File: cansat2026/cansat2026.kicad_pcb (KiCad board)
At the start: 2 copper layers, 119 parts, among them J102 MCU_UART_Conn, J103 MCU_CAM_UART_Conn, J104 920MHz_Conn, J105 I2C_Conn, J106 I2C_Conn, J117 CAM_Conn, J121 MCU_Power, J122 MCU_Power, J124 Motor_Power, J126 Micro_SD_Card_Det_Hirose_DM3AT, J201 FlightPin, J202 Heater, J301 Battery, J302 Battery, J401 M_Power_Conn, J402 M1, J403 M2, J801 Conn_Coaxial, Q301 2SB1198K, Q302 2SB1198K, Q303 2N7002, Q304 2SB1198K, Q305 2N7002, Q306 2SC2412K, Q307 PJA3404A, Q308 PJA3404A, U101 ESP32-S3-WROOM-1U-N4R8, U102 ESP32-S3-WROOM-1U-N4R8, U201 TPS564252, U202 TPS564252, U203 TPS22810DBV, U301 S-8209ABB-T8T1U, U302 S-8209ABB-T8T1U, U401 DRV8835, U601 AE-BME280, U701 BNO055 FusionModule, U801 NEO-M9N

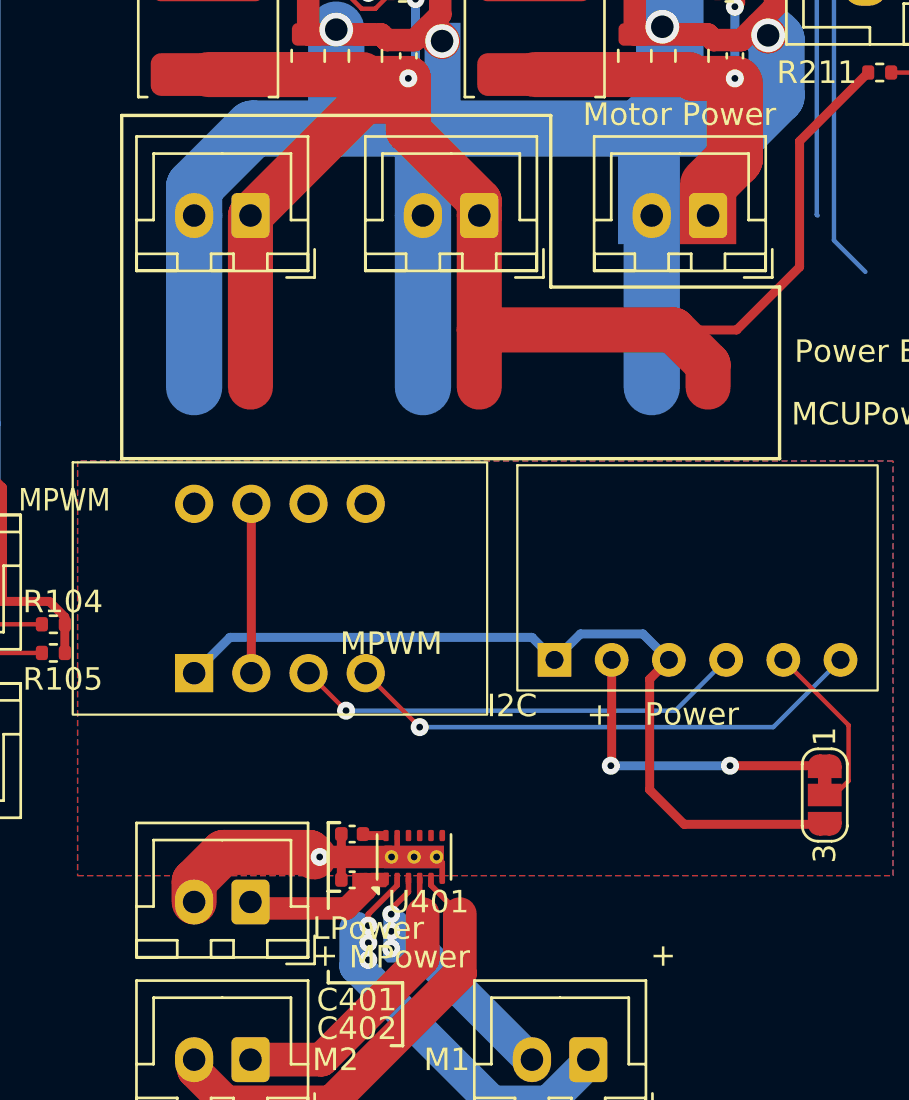
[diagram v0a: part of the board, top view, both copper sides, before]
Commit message: Update: MCUシートを作成
MCU部分を分けた
あとでFPGAつけるかもしれないしね
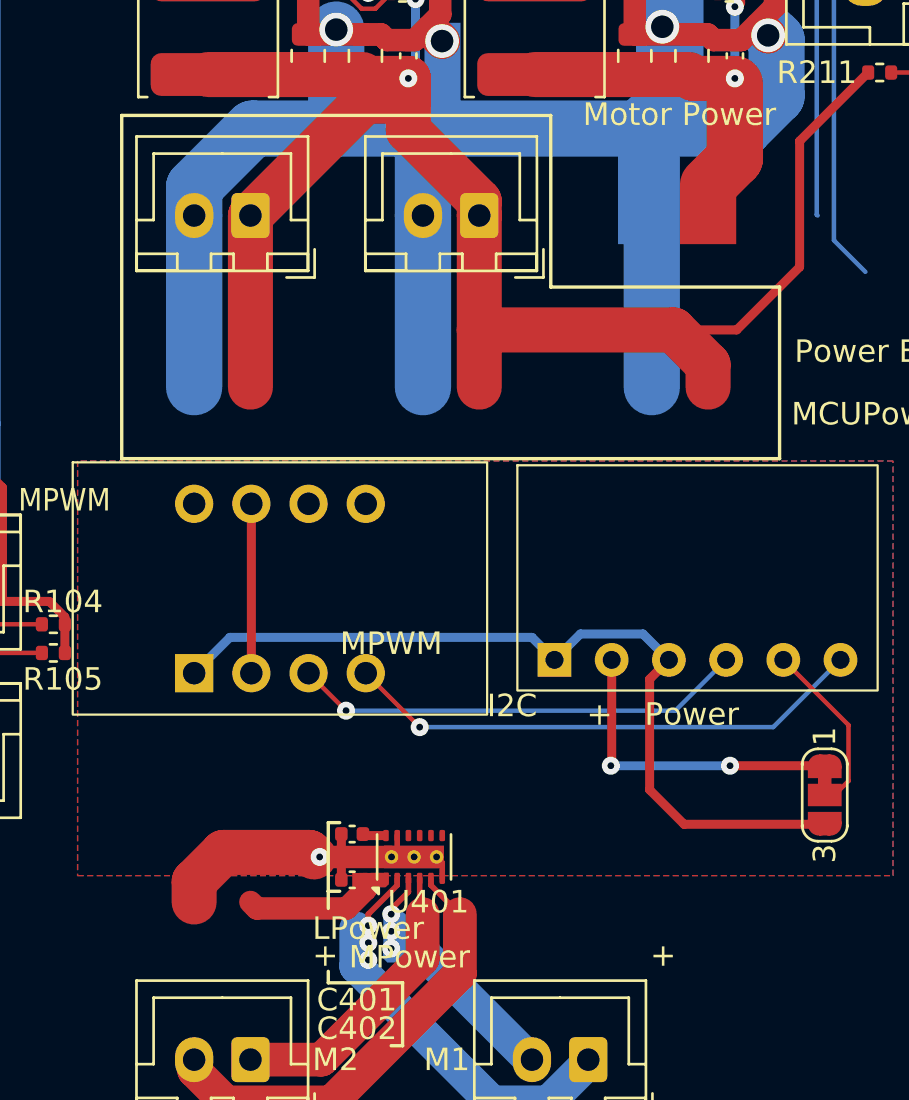
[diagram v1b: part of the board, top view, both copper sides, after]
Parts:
- removed J124: Motor_Power, Connector_JST:JST_XH_B2B-XH-A_1x02_P2.50mm_Vertical
- removed J401: M_Power_Conn, Connector_JST:JST_XH_B2B-XH-A_1x02_P2.50mm_Vertical
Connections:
- net /I2C2SCL renamed /MCU/I2C2SCL
- net /I2C2SDA renamed /MCU/I2C2SDA
- C209 pad 1: /Power/3V -> /MPWR
- C210 pad 1: /Power/3V -> /MPWR
- C211 pad 1: /Power/3V -> /MPWR
- C212 pad 1: /Power/3V -> /MPWR
- C402 pad 1: Net-(J401-Pin_1) -> /MPWR
- L202 pad 2: /Power/3V -> /MPWR
- R207 pad 1: /Power/3V -> /MPWR
- R208 pad 1: /Power/3V -> /MPWR
- U401 pad 1: Net-(J401-Pin_1) -> /MPWR
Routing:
- net /MPWR: track 0.00 -> 29.8 mm, vias 0 -> 3
- net /Power/3V: track 23.9 -> 0.00 mm, vias 3 -> 0
- net Net-(J401-Pin_1): track 5.82 -> 0.00 mm

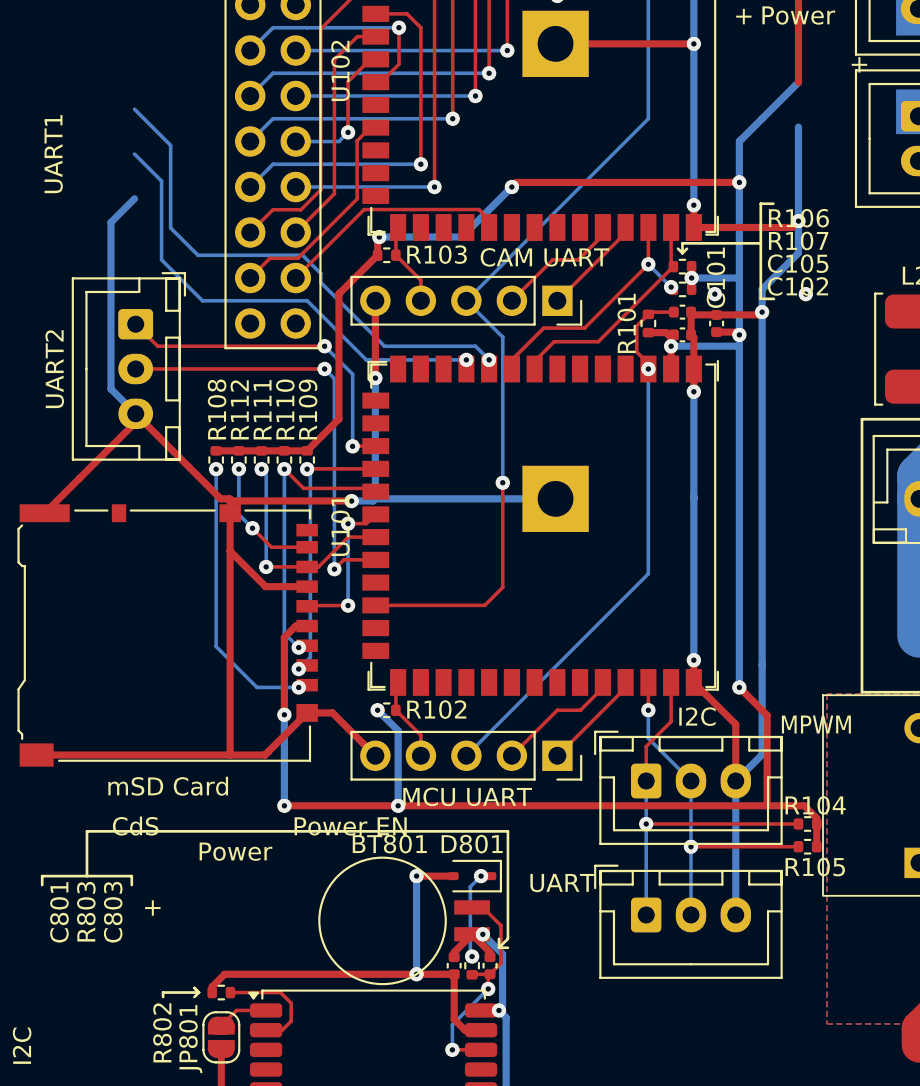
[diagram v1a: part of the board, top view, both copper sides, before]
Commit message: Update: ラベルをワイヤーにした
ラベルが衝突してERCが出たから
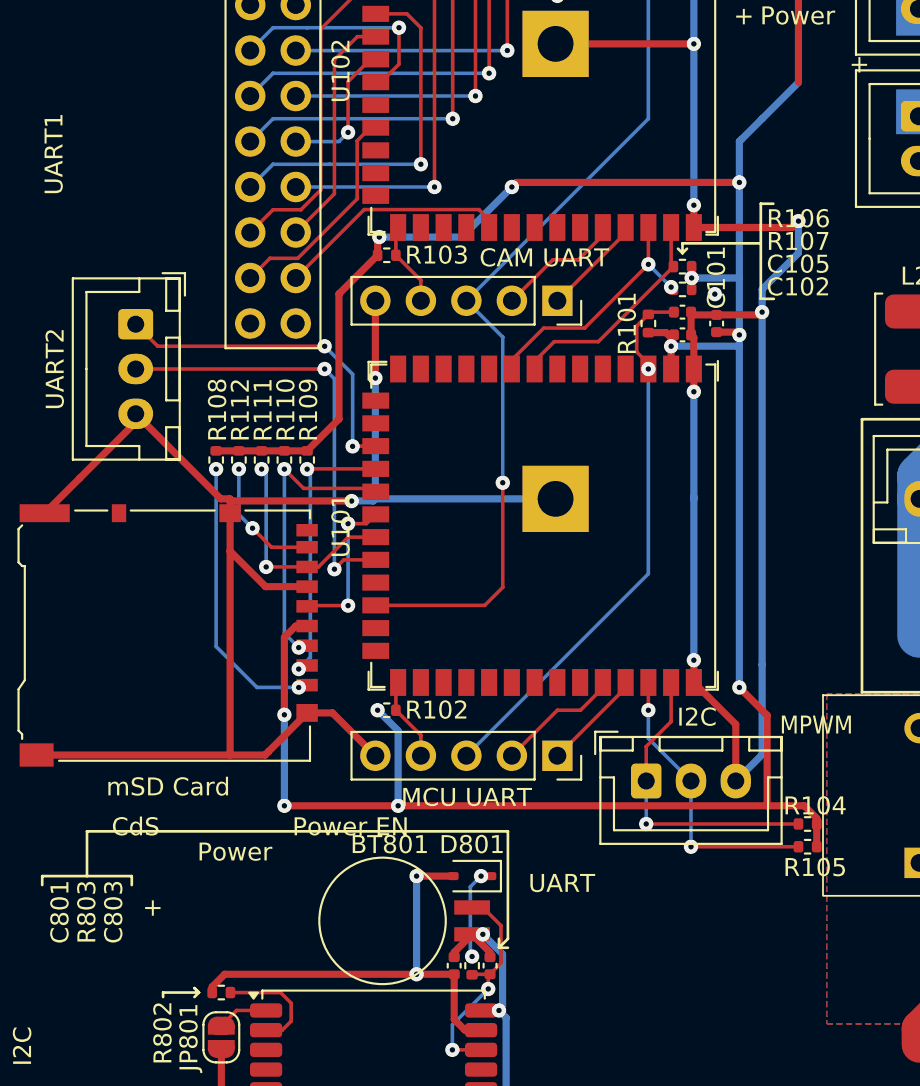
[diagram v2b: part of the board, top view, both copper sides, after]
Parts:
- removed J106: I2C_Conn, Connector_JST:JST_XH_B3B-XH-A_1x03_P2.50mm_Vertical
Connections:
- net /FP renamed /MCU/FP
- net /MA1 renamed /MCU/MA1
- net /MA2 renamed /MCU/MA2
- net /MB1 renamed /MCU/MB1
- net /MB2 renamed /MCU/MB2
- net /MPWR renamed /MD/MPWR
- net /Motor_P_EN renamed /MCU/Motor_P_EN
- net /PC_Sep renamed /MCU/PC_Sep
- net /U1RXD renamed /GPS/GPS_TX
- net /U1TXD renamed /GPS/GPS_RX
- R104 pad 2: /I2C1SDA -> /MCU/I2C1SDA
- R105 pad 2: /I2C1SCL -> /MCU/I2C1SCL
- U101 pad 38: /I2C1SCL -> /MCU/I2C1SCL
- U101 pad 39: /I2C1SDA -> /MCU/I2C1SDA
- U601 pad 4: /I2C1SDA -> /MCU/I2C1SDA
- U601 pad 6: /I2C1SCL -> /MCU/I2C1SCL
- U701 pad 3: /I2C1SDA -> /MCU/I2C1SDA
- U701 pad 4: /I2C1SCL -> /MCU/I2C1SCL
- U801 pad 18: /I2C1SDA -> /MCU/I2C1SDA
- U801 pad 19: /I2C1SCL -> /MCU/I2C1SCL
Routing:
- net /GPS/GPS_RX: track 29.1 -> 0.00 mm, vias 1 -> 0
- net /I2C1SCL: track 43.3 -> 16.2 mm, vias 3 -> 2
- net /GPS/GPS_TX: track 26.4 -> 0.00 mm, vias 1 -> 0
- net GND: track 515.5 -> 489.7 mm, vias 54 -> 53
- net /I2C1SDA: track 42.2 -> 17.0 mm, vias 2 -> 1
- net /MCU/I2C1SCL: track 0.00 -> 23.3 mm, vias 0 -> 1
- net /MCU/I2C1SDA: track 0.00 -> 20.2 mm, vias 0 -> 1

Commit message: Update: 完成した
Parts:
- removed C103: 10uF, Capacitor_SMD:C_0402_1005Metric
- removed C104: 100nF, Capacitor_SMD:C_0402_1005Metric
- removed C105: 1uF, Capacitor_SMD:C_0402_1005Metric
- removed J117: CAM_Conn, Connector_PinHeader_2.54mm:PinHeader_2x10_P2.54mm_Vertical
- removed J121, J122: MCU_Power, Connector_JST:JST_XH_B2B-XH-A_1x02_P2.50mm_Vertical
- removed J126: Micro_SD_Card_Det_Hirose_DM3AT, Connector_Card:microSD_HC_Hirose_DM3AT-SF-PEJM5
- removed J202: Heater, TerminalBlock_Phoenix:TerminalBlock_Phoenix_MKDS-1,5-2-5.08_1x02_P5.08mm_Horizontal
- removed R103, R108, R109, R110, R111, R112: 10k, Resistor_SMD:R_0402_1005Metric
- removed R104, R105, R106, R107: 4.7k, Resistor_SMD:R_0402_1005Metric
- removed R803: 1k, Resistor_SMD:R_0402_1005Metric
- removed U102: ESP32-S3-WROOM-1U-N4R8, PCM_Espressif:ESP32-S3-WROOM-1U
- added C1001: 4.7uF, Capacitor_SMD:C_0402_1005Metric, F.Cu at (99.0, 41.5)
- added C1002: 100nF, Capacitor_SMD:C_0402_1005Metric, F.Cu at (99.0, 42.5)
- added C1003: 4.7uF, Capacitor_SMD:C_0402_1005Metric, F.Cu at (109.5, 45.5)
- added C1004: 100nF, Capacitor_SMD:C_0402_1005Metric, F.Cu at (109.5, 44.5)
- added C1005: 4.7uF, Capacitor_SMD:C_0402_1005Metric, F.Cu at (97.5, 42.0)
- added C1006: 100nF, Capacitor_SMD:C_0402_1005Metric, F.Cu at (99.0, 43.5)
- added C1007: 4.7uF, Capacitor_SMD:C_0402_1005Metric, F.Cu at (96.5, 42.0)
- added C1008: 100nF, Capacitor_SMD:C_0402_1005Metric, F.Cu at (99.0, 45.0)
- added C1009: 4.7uF, Capacitor_SMD:C_0402_1005Metric, F.Cu at (103.5, 38.5)
- added C1010: 100nF, Capacitor_SMD:C_0402_1005Metric, F.Cu at (102.5, 38.5)
- added C1011: 4.7uF, Capacitor_SMD:C_0402_1005Metric, F.Cu at (108.3, 49.0)
- added C1012: 100nF, Capacitor_SMD:C_0402_1005Metric, F.Cu at (108.3, 48.0)
- added C1013: 4.7uF, Capacitor_SMD:C_0402_1005Metric, F.Cu at (100.5, 38.5)
- added C1014: 100nF, Capacitor_SMD:C_0402_1005Metric, F.Cu at (101.5, 38.5)
- added C1101: 100nF, Capacitor_SMD:C_0402_1005Metric, F.Cu at (102.5, 27.8)
- added C1102: 100nF, Capacitor_SMD:C_0402_1005Metric, F.Cu at (102.5, 31.8)
- added C1103: 100nF, Capacitor_SMD:C_0402_1005Metric, F.Cu at (102.5, 33.8)
- added C1104: 100nF, Capacitor_SMD:C_0402_1005Metric, F.Cu at (102.5, 29.8)
- added C216: 100nF, Capacitor_SMD:C_0402_1005Metric, F.Cu at (59.4, 67.7)
- added C217: 100nF, Capacitor_SMD:C_0402_1005Metric, F.Cu at (66.6, 81.8)
- added C218: 1uF, Capacitor_SMD:C_0402_1005Metric, F.Cu at (64.5, 75.2)
- added C219: 1uF, Capacitor_SMD:C_0402_1005Metric, B.Cu at (71.7, 55.0)
- added C220: 1uF, Capacitor_SMD:C_0402_1005Metric, B.Cu at (70.7, 50.9)
- added C221: 47uF, Capacitor_SMD:C_0805_2012Metric, F.Cu at (100.5, 71.0)
- added C222: 47uF, Capacitor_SMD:C_0805_2012Metric, F.Cu at (98.5, 71.0)
- added C223: 47uF, Capacitor_SMD:C_0805_2012Metric, F.Cu at (100.5, 60.9)
- added C224: 47uF, Capacitor_SMD:C_0805_2012Metric, F.Cu at (98.5, 60.9)
- added C225: 22uF, Capacitor_SMD:C_0805_2012Metric, F.Cu at (103.2, 69.0)
- added C226: 22uF, Capacitor_SMD:C_0805_2012Metric, F.Cu at (103.2, 62.8)
- added C227: 3.3nF, Capacitor_SMD:C_0603_1608Metric, F.Cu at (100.6, 64.0)
- added C228: 47uF, Capacitor_SMD:C_0805_2012Metric, F.Cu at (119.5, 72.5)
- added C229: 47uF, Capacitor_SMD:C_0805_2012Metric, F.Cu at (119.5, 74.5)
- added C230: 47uF, Capacitor_SMD:C_0805_2012Metric, F.Cu at (109.4, 72.5)
- added C231: 47uF, Capacitor_SMD:C_0805_2012Metric, F.Cu at (109.4, 74.5)
- added C232: 22uF, Capacitor_SMD:C_0805_2012Metric, F.Cu at (117.6, 69.8)
- added C233: 22uF, Capacitor_SMD:C_0805_2012Metric, F.Cu at (111.3, 69.8)
- added C234: 3.3nF, Capacitor_SMD:C_0603_1608Metric, F.Cu at (112.6, 72.3)
- added C235: 10uF, Capacitor_SMD:C_0805_2012Metric, B.Cu at (94.5, 78.2)
- added C236: 22uF, Capacitor_SMD:C_0805_2012Metric, B.Cu at (91.0, 78.2)
- added C237: 22uF, Capacitor_SMD:C_0805_2012Metric, B.Cu at (90.1, 81.0)
- added C238: 22uF, Capacitor_SMD:C_0805_2012Metric, B.Cu at (92.1, 81.0)
- added C239: 10uF, Capacitor_SMD:C_0805_2012Metric, B.Cu at (100.7, 78.9)
- added C240: 10uF, Capacitor_SMD:C_0805_2012Metric, B.Cu at (98.0, 78.2)
- added C241: 100nF, Capacitor_SMD:C_0402_1005Metric, B.Cu at (95.0, 83.3)
- added C403: 100nF, Capacitor_SMD:C_0402_1005Metric, B.Cu at (89.5, 67.0)
- added C404: 10uF, Capacitor_SMD:C_0603_1608Metric, F.Cu at (107.6, 77.0)
- added C405: 100nF, Capacitor_SMD:C_0402_1005Metric, F.Cu at (106.4, 77.0)
- added C406: 100nF, Capacitor_SMD:C_0402_1005Metric, B.Cu at (103.7, 82.0)
- added C407: 10uF, Capacitor_SMD:C_0603_1608Metric, F.Cu at (88.0, 80.2)
- added C408: 100nF, Capacitor_SMD:C_0402_1005Metric, F.Cu at (89.2, 80.0)
- added C409: 100nF, Capacitor_SMD:C_0402_1005Metric, F.Cu at (94.5, 81.0)
- added C410: 100uF, Capacitor_THT:CP_Radial_D6.3mm_P2.50mm, F.Cu at (89.0, 74.0)
- added C411: 100uF, Capacitor_THT:CP_Radial_D6.3mm_P2.50mm, F.Cu at (112.0, 80.6)
- added C412: 10uF, Capacitor_SMD:C_0603_1608Metric, F.Cu at (86.5, 80.2)
- added C601: 100nF, Capacitor_SMD:C_0402_1005Metric, F.Cu at (52.7, 75.2)
- added C701: 100nF, Capacitor_SMD:C_0402_1005Metric, F.Cu at (50.5, 68.8)
- added C702: 100nF, Capacitor_SMD:C_0402_1005Metric, F.Cu at (55.1, 68.8)
- added C901: 10uF, Capacitor_SMD:C_0402_1005Metric, F.Cu at (69.2, 45.5)
- added C902: 100nF, Capacitor_SMD:C_0402_1005Metric, F.Cu at (69.2, 46.5)
- added C903: 10uF, Capacitor_SMD:C_0402_1005Metric, B.Cu at (98.7, 35.5)
- added C904: 100nF, Capacitor_SMD:C_0402_1005Metric, B.Cu at (98.7, 34.5)
- added C905: 1uF, Capacitor_SMD:C_0402_1005Metric, B.Cu at (101.0, 35.5)
- added C906: 1uF, Capacitor_SMD:C_0402_1005Metric, F.Cu at (68.7, 44.1)
- added C907: 1uF, Capacitor_SMD:C_0402_1005Metric, B.Cu at (75.6, 56.1)
- added C908: 100nF, Capacitor_SMD:C_0402_1005Metric, F.Cu at (106.5, 52.5)
- added C909: 100nF, Capacitor_SMD:C_0402_1005Metric, F.Cu at (104.0, 52.5)
- added D1001: LED, LED_SMD:LED_0603_1608Metric, F.Cu at (117.0, 31.2)
- added D1002: LED, LED_SMD:LED_0603_1608Metric, F.Cu at (117.0, 33.0)
- added D1003: LED, LED_SMD:LED_0603_1608Metric, F.Cu at (117.0, 34.8)
- added D201: LED, LED_SMD:LED_0603_1608Metric, F.Cu at (76.0, 65.8)
- added D901: LED, LED_SMD:LED_0603_1608Metric, F.Cu at (78.4, 81.5)
- added D902: LED, LED_SMD:LED_0603_1608Metric, F.Cu at (78.4, 79.5)
- added D903: LED, LED_SMD:LED_0603_1608Metric, F.Cu at (78.4, 77.8)
- added G***: LOGO, LOGO, F.Cu at (110.5, 60.8)
- added G***: LOGO, LOGO, F.Cu at (110.5, 66.8)
- added G***: LOGO, LOGO, B.Cu at (113.5, 60.8)
- added J101: MCU_UART_Conn, Connector_PinSocket_2.54mm:PinSocket_1x05_P2.54mm_Vertical, F.Cu at (92.7, 30.2)
- added J106: MCU_Power, Connector_JST:JST_XH_B2B-XH-A_1x02_P2.50mm_Vertical, F.Cu at (74.7, 48.2)
- added J107: Micro_SD_Card_Det_Hirose_DM3AT, Connector_Card:microSD_HC_Hirose_DM3AT-SF-PEJM5, F.Cu at (55.4, 30.8)
- added J1101: USB_C_Receptacle_USB2.0_14P, Connector_USB:USB_C_Receptacle_GCT_USB4105-xx-A_16P_TopMnt_Horizontal, F.Cu at (96.0, 23.4)
- added J1102: USB_C_Receptacle_USB2.0_14P, Connector_USB:USB_C_Receptacle_GCT_USB4105-xx-A_16P_TopMnt_Horizontal, F.Cu at (109.0, 23.4)
- added J401: M1, Connector_JST:JST_VH_B2P-VH_1x02_P3.96mm_Vertical, F.Cu at (87.5, 65.2)
- added JP1001: I2C Addr, Jumper:SolderJumper-3_P1.3mm_Bridged12_RoundedPad1.0x1.5mm_NumberLabels, F.Cu at (98.7, 49.0)
- added JP701: I2C Addr, Jumper:SolderJumper-3_P1.3mm_Bridged12_RoundedPad1.0x1.5mm_NumberLabels, F.Cu at (43.0, 50.0)
- added L203: 1uH, Inductor_SMD:L_Wuerth_PMCI-252010, F.Cu at (103.2, 71.5)
- added L204: 1uH, Inductor_SMD:L_Wuerth_PMCI-252010, F.Cu at (103.2, 60.4)
- added L205: 1uH, Inductor_SMD:L_Wuerth_PMCI-252010, F.Cu at (120.0, 69.8)
- added L206: 1uH, Inductor_SMD:L_Wuerth_PMCI-252010, F.Cu at (108.9, 69.8)
- added L207: 1.5uH, Inductor_SMD:L_Wuerth_PMCI-201610, B.Cu at (96.2, 76.0)
- added Q1101: 2N7002, Package_TO_SOT_SMD:SOT-23, B.Cu at (94.2, 22.0)
- added Q1102: 2N7002, Package_TO_SOT_SMD:SOT-23, B.Cu at (97.7, 22.0)
- added Q1103: 2N7002, Package_TO_SOT_SMD:SOT-23, B.Cu at (107.2, 22.0)
- added Q1104: 2N7002, Package_TO_SOT_SMD:SOT-23, B.Cu at (110.7, 22.0)
- added R1001: 100, Resistor_SMD:R_0402_1005Metric, F.Cu at (99.0, 40.5)
- added R1002: 10k, Resistor_SMD:R_0402_1005Metric, B.Cu at (106.0, 56.2)
- added R1003: 3.3k, Resistor_SMD:R_0402_1005Metric, B.Cu at (103.8, 56.2)
- added R1004: 1k, Resistor_SMD:R_0402_1005Metric, F.Cu at (114.5, 31.2)
- added R1005: 1k, Resistor_SMD:R_0402_1005Metric, F.Cu at (114.5, 33.0)
- added R1006: 1k, Resistor_SMD:R_0402_1005Metric, F.Cu at (114.5, 34.8)
- added R1101: 5.1k, Resistor_SMD:R_0402_1005Metric, B.Cu at (93.0, 24.5)
- added R1102: 5.1k, Resistor_SMD:R_0402_1005Metric, B.Cu at (99.0, 24.5)
- added R1103: 5.1k, Resistor_SMD:R_0402_1005Metric, B.Cu at (106.0, 24.5)
- added R1104: 5.1k, Resistor_SMD:R_0402_1005Metric, B.Cu at (112.0, 24.5)
- added R213: 100k, Resistor_SMD:R_0402_1005Metric, F.Cu at (91.6, 50.8)
- added R214: 100k, Resistor_SMD:R_0402_1005Metric, F.Cu at (90.6, 50.8)
- added R215: 470k, Resistor_SMD:R_0402_1005Metric, F.Cu at (98.4, 64.0)
- added R216: 150k, Resistor_SMD:R_0402_1005Metric, F.Cu at (99.3, 64.0)
- added R217: 470k, Resistor_SMD:R_0402_1005Metric, F.Cu at (112.6, 74.5)
- added R218: 100k, Resistor_SMD:R_0402_1005Metric, F.Cu at (76.0, 63.5)
- added R219: 150k, Resistor_SMD:R_0402_1005Metric, F.Cu at (112.6, 73.6)
- added R220: 330k, Resistor_SMD:R_0402_1005Metric, B.Cu at (93.6, 80.7)
- added R221: 100k, Resistor_SMD:R_0402_1005Metric, B.Cu at (98.8, 80.1)
- added R222: 51k, Resistor_SMD:R_0402_1005Metric, B.Cu at (93.6, 82.5)
- added R901: 10k, Resistor_SMD:R_0402_1005Metric, B.Cu at (101.0, 34.5)
- added R902: 10k, Resistor_SMD:R_0402_1005Metric, F.Cu at (69.7, 44.1)
- added R903: 100k, Resistor_SMD:R_0402_1005Metric, F.Cu at (63.8, 28.1)
- added R904: 10k, Resistor_SMD:R_0402_1005Metric, F.Cu at (56.2, 68.8)
- added R905: 10k, Resistor_SMD:R_0402_1005Metric, B.Cu at (115.0, 56.0)
- added R906: 4.7k, Resistor_SMD:R_0402_1005Metric, F.Cu at (68.7, 67.7)
- added R907: 4.7k, Resistor_SMD:R_0402_1005Metric, F.Cu at (67.4, 67.7)
- added R908: 4.7k, Resistor_SMD:R_0402_1005Metric, F.Cu at (61.1, 46.0)
- added R909: 4.7k, Resistor_SMD:R_0402_1005Metric, F.Cu at (59.8, 46.0)
- added R910: 4.7k, Resistor_SMD:R_0402_1005Metric, F.Cu at (50.7, 60.8)
- added R911: 10k, Resistor_SMD:R_0402_1005Metric, F.Cu at (50.7, 53.2)
- added R912: 10k, Resistor_SMD:R_0402_1005Metric, F.Cu at (50.7, 55.5)
- added R913: 10k, Resistor_SMD:R_0402_1005Metric, F.Cu at (50.7, 58.0)
- added R914: 1k, Resistor_SMD:R_0402_1005Metric, F.Cu at (76.4, 81.3)
- added R915: 1k, Resistor_SMD:R_0402_1005Metric, F.Cu at (76.4, 79.5)
- added R916: 1k, Resistor_SMD:R_0402_1005Metric, F.Cu at (76.4, 77.5)
- added R917: 10k, Resistor_SMD:R_0402_1005Metric, F.Cu at (103.0, 35.5)
- added R918: 200k, Resistor_SMD:R_0402_1005Metric, F.Cu at (106.5, 53.5)
- added R919: 150k, Resistor_SMD:R_0402_1005Metric, F.Cu at (95.8, 46.7)
- added R920: 4.7k, Resistor_SMD:R_0402_1005Metric, F.Cu at (106.5, 48.5)
- added R921: 4.7k, Resistor_SMD:R_0402_1005Metric, F.Cu at (106.5, 49.5)
- added R923: 200k, Resistor_SMD:R_0402_1005Metric, F.Cu at (104.0, 53.5)
- added R924: 10k, Resistor_SMD:R_0402_1005Metric, F.Cu at (104.0, 48.5)
- added R925: 10k, Resistor_SMD:R_0402_1005Metric, F.Cu at (104.0, 49.5)
- added REF**: ToolingHole_2mm, Project:ToolingHole_2mm, F.Cu at (126.5, 24.8)
- added REF**: MountingHole_3.2mm_M3, MountingHole:MountingHole_3.2mm_M3, F.Cu at (86.0, 85.8)
- added REF**: Fiducial_1mm_Mask2mm, Fiducial:Fiducial_1mm_Mask2mm, F.Cu at (125.1, 79.8)
- added REF**: Fiducial_1mm_Mask2mm, Fiducial:Fiducial_1mm_Mask2mm, F.Cu at (36.8, 29.8)
- added REF**: Fiducial_1mm_Mask2mm, Fiducial:Fiducial_1mm_Mask2mm, F.Cu at (125.1, 29.8)
- added REF**: MountingHole_3.2mm_M3, MountingHole:MountingHole_3.2mm_M3, F.Cu at (44.0, 85.8)
- added REF**: Mousebite_5x2mm_dual, Project:Mousebite_5x2mm_dual, F.Cu at (80.0, 74.8)
- added REF**: Mousebite_5x2mm, Project:Mousebite_5x2mm, F.Cu at (40.0, 34.8)
- added REF**: Mousebite_5x2mm_dual, Project:Mousebite_5x2mm_dual, F.Cu at (80.0, 34.8)
- added REF**: MountingHole_3.2mm_M3, MountingHole:MountingHole_3.2mm_M3, F.Cu at (44.0, 23.8)
- added REF**: JST_VH_B2P-VH_1x02_P3.96mm_Vertical, Connector_JST:JST_VH_B2P-VH_1x02_P3.96mm_Vertical, F.Cu at (87.5, 54.5)
- added REF**: Fiducial_1mm_Mask2mm, Fiducial:Fiducial_1mm_Mask2mm, F.Cu at (36.8, 79.8)
- added REF**: PinHeader_2x10_P1.27mm_Vertical, Connector_PinHeader_1.27mm:PinHeader_2x10_P1.27mm_Vertical, F.Cu at (74.5, 29.8)
- added REF**: Mousebite_5x2mm, Project:Mousebite_5x2mm, F.Cu at (122.0, 34.8)
- added REF**: JST_VH_B2P-VH_1x02_P3.96mm_Vertical, Connector_JST:JST_VH_B2P-VH_1x02_P3.96mm_Vertical, F.Cu at (75.5, 69.8)
- added REF**: MountingHole_3.2mm_M3, MountingHole:MountingHole_3.2mm_M3, F.Cu at (86.0, 23.8)
- added REF**: MountingHole_3.2mm_M3, MountingHole:MountingHole_3.2mm_M3, F.Cu at (76.0, 23.8)
- added REF**: ToolingHole_2mm, Project:ToolingHole_2mm, F.Cu at (35.5, 84.8)
- added REF**: Mousebite_5x2mm, Project:Mousebite_5x2mm, F.Cu at (40.0, 74.8)
- added REF**: ToolingHole_2mm, Project:ToolingHole_2mm, F.Cu at (126.5, 84.8)
- added REF**: PinHeader_2x10_P1.27mm_Vertical, Connector_PinHeader_1.27mm:PinHeader_2x10_P1.27mm_Vertical, F.Cu at (84.0, 29.8)
- added REF**: ToolingHole_2mm, Project:ToolingHole_2mm, F.Cu at (35.5, 24.8)
- added REF**: MountingHole_3.2mm_M3, MountingHole:MountingHole_3.2mm_M3, F.Cu at (118.0, 85.8)
- added REF**: MountingHole_3.2mm_M3, MountingHole:MountingHole_3.2mm_M3, F.Cu at (118.0, 23.8)
- added REF**: MountingHole_3.2mm_M3, MountingHole:MountingHole_3.2mm_M3, F.Cu at (76.0, 85.8)
- added REF**: Mousebite_5x2mm, Project:Mousebite_5x2mm, F.Cu at (122.0, 74.8)
- added RV201: 200k, Potentiometer_SMD:Potentiometer_Bourns_TC33X_Vertical, F.Cu at (98.7, 67.4)
- added RV202: 200k, Potentiometer_SMD:Potentiometer_Bourns_TC33X_Vertical, F.Cu at (116.0, 74.2)
- added SW201: SW_SPST, Button_Switch_SMD:SW_DIP_SPSTx01_Slide_6.7x4.1mm_W8.61mm_P2.54mm_LowProfile, F.Cu at (75.5, 57.2)
- added SW901: SW_SPST, Project:IS-1235-G, F.Cu at (67.9, 24.4)
- added U1001: ICE40UP5K-SG48ITR, Package_DFN_QFN:QFN-48-1EP_7x7mm_P0.5mm_EP5.6x5.6mm, F.Cu at (104.2, 43.8)
- added U1101: USBLC6-2SC6, Package_TO_SOT_SMD:SOT-23-6, B.Cu at (96.0, 25.5)
- added U1102: CH340K, Package_SO:SSOP-10-1EP_3.9x4.9mm_P1mm_EP2.1x3.3mm, F.Cu at (98.2, 31.2)
- added U1103: USBLC6-2SC6, Package_TO_SOT_SMD:SOT-23-6, B.Cu at (109.0, 25.5)
- added U1104: CH340K, Package_SO:SSOP-10-1EP_3.9x4.9mm_P1mm_EP2.1x3.3mm, F.Cu at (106.7, 31.2)
- added U204: 74HC08, Package_SO:SOIC-14_3.9x8.7mm_P1.27mm, B.Cu at (75.5, 61.2)
- added U205: INA226, Package_SO:TSSOP-10_3x3mm_P0.5mm, F.Cu at (67.3, 85.3)
- added U206: TPS562242, Package_TO_SOT_SMD:SOT-563, F.Cu at (62.8, 74.2)
- added U207: XC6206P332MR, Package_TO_SOT_SMD:SOT-23-3, B.Cu at (70.2, 53.5)
- added U208: TPS62180, Project:TPS62180YZF, F.Cu at (102.9, 65.9)
- added U209: TPS62180, Project:TPS62180YZF, F.Cu at (114.5, 70.0)
- added U210: TPS63070, Project:QFN-16_2.4x2.9_Pitch0.5mm, B.Cu at (96.2, 81.0)
- added U402: TC78H653FTG, Package_DFN_QFN:VQFN-16-1EP_3x3mm_P0.5mm_EP1.8x1.8mm, F.Cu at (103.7, 77.5)
- added U403: AM8068, Package_TO_SOT_SMD:SOT-23-6, F.Cu at (92.0, 80.5)
- added U901: ESP32-S3-WROOM-1U-N4R8, PCM_Espressif:ESP32-S3-WROOM-1U, F.Cu at (61.7, 56.9)
- added U902: ESP32-S3-WROOM-1U-N4R8, PCM_Espressif:ESP32-S3-WROOM-1U, B.Cu at (106.2, 45.8)
- added U903: AW9523B, Package_DFN_QFN:QFN-24-1EP_4x4mm_P0.5mm_EP2.7x2.7mm, B.Cu at (75.5, 52.8)
- added U904: PCA9306DQER, Package_SON:X2SON-8_1.4x1mm_P0.35mm, F.Cu at (106.5, 51.0)
- added U905: PCA9306DQER, Package_SON:X2SON-8_1.4x1mm_P0.35mm, F.Cu at (104.0, 51.0)
- BT801: value MS621FE FL11E -> MS621R II27E; footprint Battery:BatteryHolder_Seiko_MS621F -> Project:BAT_MS621R-II27E; moved to B.Cu
- C101: value 10uF -> 100nF; moved to B.Cu
- C102, C803, JP801, L801: moved to B.Cu
- C201: value 10uF -> 1uF; footprint Capacitor_SMD:C_0805_2012Metric -> Capacitor_SMD:C_0402_1005Metric
- C202: value 100nF -> 2.2uF; footprint Capacitor_SMD:C_0603_1608Metric -> Capacitor_SMD:C_0402_1005Metric
- C203: value 30pF -> 100nF
- C204: value 22uF -> 100nF; footprint Capacitor_SMD:C_0805_2012Metric -> Capacitor_SMD:C_0402_1005Metric
- C205, C210, C211: value 22uF -> 10uF
- C207: value 10uF -> 22uF
- C208: footprint Capacitor_SMD:C_0603_1608Metric -> Capacitor_SMD:C_0402_1005Metric; moved to B.Cu
- C209: value 30pF -> 10uF
- C213: value 1uF -> 100nF
- C214: value 100nF -> 33pF; footprint Capacitor_SMD:C_0603_1608Metric -> Capacitor_SMD:C_0402_1005Metric
- C215: value 2200pF -> 22uF; footprint Capacitor_SMD:C_0402_1005Metric -> Capacitor_SMD:C_0805_2012Metric
- C301, C303: footprint Capacitor_SMD:C_0603_1608Metric -> Capacitor_SMD:C_0402_1005Metric
- C401: value 100nF -> 10uF; footprint Capacitor_SMD:C_0402_1005Metric -> Capacitor_SMD:C_0603_1608Metric
- C801: value 10uF -> 10nF(X7R); moved to B.Cu
- C802: value 100nF(X7R) -> 10uF; moved to B.Cu
- D801: value CUS10F30 -> 1N5819WS; moved to B.Cu
- J102: value MCU_UART_Conn -> CAM_Conn; footprint Connector_PinSocket_2.54mm:PinSocket_1x05_P2.54mm_Vertical -> Project:SHOUHAN_XJH2.0_0.43-24P_1x24-1MP_P0.50mm_Horizontal
- J104: value 920MHz_Conn -> I2C_Conn
- J105: value I2C_Conn -> MCU_Power; footprint Connector_JST:JST_XH_B3B-XH-A_1x03_P2.50mm_Vertical -> Connector_JST:JST_XH_B2B-XH-A_1x02_P2.50mm_Vertical
- J301, J302: footprint Connector_JST:JST_XH_B2B-XH-A_1x02_P2.50mm_Vertical -> Connector_JST:JST_VH_B2P-VH_1x02_P3.96mm_Vertical
- J402: value M1 -> M2; footprint Connector_JST:JST_XH_B2B-XH-A_1x02_P2.50mm_Vertical -> Connector_JST:JST_VH_B2P-VH_1x02_P3.96mm_Vertical
- J403: value M2 -> M3
- J801: footprint Connector_Coaxial:SMA_Amphenol_132134-11_Vertical -> Connector_Coaxial:U.FL_Hirose_U.FL-R-SMT-1_Vertical; moved to B.Cu
- L201: value 3.3uH -> 4.7uH; footprint Inductor_SMD:L_TDK_VLS6045EX_VLS6045AF -> Inductor_SMD:L_Wuerth_PMCI-252012
- L202: value 3.3uH -> 2.2uH; footprint Inductor_SMD:L_TDK_VLS6045EX_VLS6045AF -> Inductor_SMD:L_Taiyo-Yuden_NR-50xx
- R201: value 33k -> 10k; moved to B.Cu
- R202: value 100k -> 39k
- R204: value 12k -> 10
- R205: value 30k -> 15k; footprint Resistor_SMD:R_0603_1608Metric -> Resistor_SMD:R_0402_1005Metric
- R206: value 10k -> 10m; footprint Resistor_SMD:R_0402_1005Metric -> Resistor_SMD:R_1206_3216Metric
- R207: value 20k -> 47k
- R208, R212: value 10k -> 100k
- R209: value 20k -> 10
- R210: value 10k -> 1k
- R211: value 10k -> 20k
- R801: value 200(0.125W) -> 10(0.25W); footprint Resistor_SMD:R_0805_2012Metric -> Resistor_SMD:R_1206_3216Metric; moved to B.Cu
- R802: value 10k -> 1k; moved to B.Cu
- U101: value ESP32-S3-WROOM-1U-N4R8 -> E220-900T22S(JP); footprint PCM_Espressif:ESP32-S3-WROOM-1U -> Project:E220-900T22S(JP); moved to B.Cu
- U201: value TPS564252 -> TPS70912DRVR; footprint Package_TO_SOT_SMD:SOT-563 -> Package_SON:WSON-6-1EP_2x2mm_P0.65mm_EP1x1.6mm
- U202: value TPS564252 -> TCR2LN18; footprint Package_TO_SOT_SMD:SOT-563 -> Project:SDFN4
- U203: value TPS22810DBV -> TPS561201DDC
- U401: value DRV8835 -> TC78H653FTG; footprint Package_SON:WSON-12-1EP_3x2mm_P0.5mm_EP1x2.65_ThermalVias -> Package_DFN_QFN:VQFN-16-1EP_3x3mm_P0.5mm_EP1.8x1.8mm
- U601: value AE-BME280 -> HP203B; footprint Project:AE-BME280 -> Project:HP203B
- U701: value BNO055 FusionModule -> LSM6DSV; footprint Project:BNO055-FusionModule -> Package_LGA:LGA-14_3x2.5mm_P0.5mm_LayoutBorder3x4y
- U801: value NEO-M9N -> MAX-M10S; footprint RF_GPS:ublox_NEO -> RF_GPS:ublox_MAX; moved to B.Cu
- moved JP601 153.9 mm to (43.0, 52.5), turned to 180 degrees
- moved J201 147.2 mm to (44.5, 31.0)
- moved R201 130.3 mm to (42.9, 31.6), turned to 90 degrees
- moved U601 123.4 mm to (52.7, 72.2)
- moved R303 123.1 mm to (46.4, 58.3), turned to 180 degrees
- moved R304 122.8 mm to (46.4, 63.0), turned to 180 degrees
- moved R316 122.4 mm to (50.9, 77.2), turned to 90 degrees
- moved R310 121.7 mm to (43.6, 58.3), turned to 0 degrees
- moved Q301 121.4 mm to (47.9, 55.9), turned to 90 degrees
- moved R314 121.3 mm to (44.7, 76.5)
- moved R313 121.3 mm to (41.7, 55.9), turned to -90 degrees
- moved Q305 120.8 mm to (43.2, 75.0), turned to -90 degrees
- moved Q302 120.7 mm to (47.9, 60.6), turned to 90 degrees
- moved Q308 119.7 mm to (53.2, 77.8), turned to 0 degrees
- moved R211 119.3 mm to (64.4, 72.7), turned to 180 degrees
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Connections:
- C101 pad 1: /VCC -> /3.8V
- C102 pad 1: /VCC -> /COM_AUX
- C201 pad 1: /Power/VIN -> VIN
- C202 pad 1: /Power/VIN -> /1.2V
- C203 pad 2: Net-(U201-FB) -> GND
- C204 pad 1: /VCC -> /1.8V
- C205 pad 1: /VCC -> VIN
- C206 pad 1: /VCC -> Net-(U203-SW)
- C206 pad 2: GND -> Net-(U203-VBST)
- C207 pad 1: /Power/VIN -> /3.8V
- C208 pad 1: /Power/VIN -> /Power/3.3V_AUX
- C209 pad 1: /MD/MPWR -> /VCC
- C209 pad 2: Net-(U202-FB) -> GND
- C210 pad 1: /MD/MPWR -> VIN
- C211 pad 1: /MD/MPWR -> VIN
- C212 pad 1: /MD/MPWR -> VIN
- C213 pad 1: /Power/VIN -> Net-(U206-SW)
- C213 pad 2: GND -> Net-(U206-BST)
- C214 pad 1: Net-(J202-Pin_1) -> /VCC
- C214 pad 2: GND -> Net-(U206-FB)
- C215 pad 1: Net-(U203-CT) -> /VCC
- C401 pad 1: /VCC -> /MD/M1PWR
- C402 pad 1: /MD/MPWR -> /MD/M1PWR
- C801 pad 1: /VCC -> Net-(C801-Pad1)
- C802 pad 1: Net-(C802-Pad1) -> /VCC
- J102 pad 1: /U0TXD -> /VCC
- J102 pad 2: /U0RXD -> /VCC
- J102 pad 3: /EN -> /CAM_PIN_SIOC
- J102 pad 4: /GPIO0 -> /CAM_PIN_SIOD
- J102 pad 5: GND -> /CAM_PIN_PWDN
- J104 pad 1: /U2TXD -> /I2C1SDA
- J104 pad 2: /U2RXD -> /I2C1SCL
- J105 pad 1: /I2C1SDA -> /VCC
- J105 pad 2: /I2C1SCL -> GND
- J301 pad 1: /Power/VIN -> /Power/BATT+
- L201 pad 1: Net-(U201-SW) -> Net-(U203-SW)
- L201 pad 2: /VCC -> /3.8V
- L202 pad 1: Net-(U202-SW) -> Net-(U206-SW)
- L202 pad 2: /MD/MPWR -> /VCC
- L801 pad 1: Net-(C802-Pad1) -> Net-(C801-Pad1)
- Q301 pad 2: /Power/VIN -> /Power/BATT+
- Q302 pad 2: /Power/VIN -> /Power/BATT+
- Q304 pad 2: /Power/VIN -> /Power/BATT+
- R101 pad 2: /EN -> /SD_DAT2
- R102 pad 2: /GPIO0 -> /SD_DAT1
- R201 pad 2: Net-(R201-Pad2) -> /MCU/FP
- R202 pad 1: /Power/VIN -> /3.8V
- R202 pad 2: Net-(U201-EN) -> Net-(U203-VFB)
- R203 pad 1: /VCC -> Net-(U203-VFB)
- R203 pad 2: Net-(U201-PG) -> GND
- R204 pad 1: Net-(R201-Pad2) -> /Power/BATT+
- R204 pad 2: Net-(U201-FB) -> Net-(U205-Vin+)
- R205 pad 1: Net-(U201-EN) -> /VCC
- R205 pad 2: GND -> Net-(R205-Pad2)
- R206 pad 1: Net-(U201-FB) -> /Power/BATT+
- R206 pad 2: GND -> VIN
- R207 pad 1: /MD/MPWR -> Net-(R205-Pad2)
- R207 pad 2: Net-(R207-Pad2) -> Net-(U206-FB)
- R208 pad 1: /MD/MPWR -> Net-(U206-EN)
- R208 pad 2: Net-(U202-PG) -> /Power/MASTER_EN
- R209 pad 1: Net-(R207-Pad2) -> VIN
- R209 pad 2: Net-(U202-FB) -> Net-(U205-Vin-)
- R210 pad 1: Net-(U202-FB) -> Net-(D201-K)
- R211 pad 1: /VCC -> Net-(U206-FB)
- R211 pad 2: /MCU/FP -> GND
- R212 pad 1: /MCU/PC_Sep -> /VCC
- R212 pad 2: GND -> /Power/M1PG
- R301 pad 1: /Power/VIN -> /Power/BATT+
- R302 pad 1: /Power/VIN -> /Power/BATT+
- R305 pad 2: /Power/VIN -> /Power/BATT+
- R306 pad 2: /Power/VIN -> /Power/BATT+
- R310 pad 2: /Power/VIN -> /Power/BATT+
- R801 pad 2: Net-(C802-Pad1) -> Net-(C801-Pad1)
- R802 pad 1: /VCC -> Net-(D801-K)
- R802 pad 2: Net-(U801-D_SEL) -> /GPS/V_BCKP
- U101 pad 10: /GPS/GPS_RX -> /3.8V
- U101 pad 11: /GPS/GPS_TX -> GND
- U101 pad 17: /U2TXD -> unconnected-(U101-NC-Pad17)
- U101 pad 18: /SPI2CS0 -> unconnected-(U101-NC-Pad18)
- U101 pad 19: /SPI2MOSI -> GND
- U101 pad 2: /VCC -> GND
- U101 pad 20: /SPI2SCLK -> GND
- U101 pad 21: /SPI2MISO -> unconnected-(U101-ANT-Pad21)
- U101 pad 22: /U2RXD -> GND
- U101 pad 3: /EN -> GND
- U101 pad 4: /MCU/MA1 -> GND
- U101 pad 5: /MCU/MA2 -> /COM_M0
- U101 pad 6: /MCU/MB1 -> /COM_M1
- U101 pad 7: /MCU/MB2 -> /U2TXD
- U101 pad 8: /MCU/I2C2SDA -> /U2RXD
- U101 pad 9: /MCU/I2C2SCL -> /COM_AUX
- U201 pad 1: /Power/VIN -> /1.2V
- U201 pad 2: Net-(U201-SW) -> unconnected-(U201-NC-Pad2)
- U201 pad 4: Net-(U201-PG) -> /Power/MASTER_EN
- U201 pad 5: Net-(U201-EN) -> unconnected-(U201-NC-Pad5)
- U201 pad 6: Net-(U201-FB) -> VIN
- U202 pad 1: /Power/VIN -> /1.8V
- U202 pad 2: Net-(U202-SW) -> GND
- U202 pad 3: GND -> /VCC
- U202 pad 4: Net-(U202-PG) -> /VCC
- U202 pad 5: /MCU/Motor_P_EN -> unconnected-(U202-NC-Pad5)
- U203 pad 1: /Power/VIN -> GND
- U203 pad 2: GND -> Net-(U203-SW)
- U203 pad 3: /MCU/PC_Sep -> VIN
- U203 pad 4: Net-(U203-CT) -> Net-(U203-VFB)
- U203 pad 5: Net-(J202-Pin_1) -> Net-(U203-EN)
- U203 pad 6: Net-(J202-Pin_1) -> Net-(U203-VBST)
- U401 pad 1: /MD/MPWR -> unconnected-(U401-IN4-Pad1)
- U401 pad 10: /MCU/MA1 -> Net-(J401-Pin_1)
- U401 pad 11: GND -> Net-(J401-Pin_2)
- U401 pad 12: /VCC -> Net-(J401-Pin_2)
- U401 pad 2: Net-(J402-Pin_1) -> unconnected-(U401-IN3-Pad2)
- U401 pad 3: Net-(J402-Pin_2) -> unconnected-(U401-NC-Pad3)
- U401 pad 4: Net-(J403-Pin_1) -> /MCU/MA1
- U401 pad 5: Net-(J403-Pin_2) -> /MCU/MA2
- U401 pad 6: GND -> /MD/M1-2_EN
- U401 pad 7: /MCU/MB2 -> unconnected-(U401-NC-Pad7)
- U401 pad 8: /MCU/MB1 -> GND
- U401 pad 9: /MCU/MA2 -> Net-(J401-Pin_1)
- U601 pad 1: /VCC -> unconnected-(U601-INT1-Pad1)
- U601 pad 4: /MCU/I2C1SDA -> unconnected-(U601-NC-Pad4)
- U601 pad 5: Net-(JP601-C) -> /I2C1SCL
- U601 pad 6: /MCU/I2C1SCL -> /I2C1SDA
- U701 pad 1: /VCC -> Net-(JP701-C)
- U701 pad 3: /MCU/I2C1SDA -> GND
- U701 pad 4: /MCU/I2C1SCL -> unconnected-(U701-INT1-Pad4)
- U701 pad 5: unconnected-(U701-~{RESET}-Pad5) -> /VCC
- U701 pad 6: unconnected-(U701-INT-Pad6) -> GND
- U701 pad 8: unconnected-(U701-VOUT-Pad8) -> /VCC
- U801 pad 1: Net-(JP801-B) -> GND
- U801 pad 13: GND -> unconnected-(U801-LNA_EN-Pad13)
- U801 pad 14: unconnected-(U801-LNA_EN-Pad14) -> Net-(U801-VCC_RF)
- U801 pad 16: unconnected-(U801-RESERVED-Pad16) -> /I2C1SDA
- U801 pad 17: unconnected-(U801-RESERVED-Pad17) -> /I2C1SCL
- U801 pad 18: /MCU/I2C1SDA -> Net-(JP801-B)
- U801 pad 2: Net-(U801-D_SEL) -> /GPS/GPS_TX
- U801 pad 3: unconnected-(U801-TIMEPULSE-Pad3) -> /GPS/GPS_RX
- U801 pad 6: unconnected-(U801-USB_DP-Pad6) -> /GPS/V_BCKP
- U801 pad 7: GND -> /VCC
- U801 pad 8: unconnected-(U801-~{RESET}-Pad8) -> /VCC
- U801 pad 9: Net-(U801-VCC_RF) -> unconnected-(U801-~{RESET}-Pad9)
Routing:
- net GND: track 489.7 -> 225.1 mm, vias 53 -> 434
- net /VCC: track 328.6 -> 119.7 mm, vias 17 -> 40
- net Net-(U208-EN): track 0.00 -> 97.2 mm, vias 0 -> 4
- net /MD/M1-2_EN: track 0.00 -> 93.3 mm, vias 0 -> 6
- net Net-(U210-EN): track 0.00 -> 90.3 mm, vias 0 -> 5
- net /I2C1SDA: track 17.0 -> 107.2 mm, vias 1 -> 7
- net /I2C1SCL: track 16.2 -> 103.6 mm, vias 2 -> 7
- net /Power/MASTER_EN: track 0.00 -> 84.8 mm, vias 0 -> 5
- net /GPIO0: track 4.72 -> 89.4 mm, vias 0 -> 5
- net /Power/M2PG: track 0.00 -> 81.9 mm, vias 0 -> 3
- net /MCU/MC2: track 0.00 -> 79.2 mm, vias 0 -> 1
- net /MCU/MC1: track 0.00 -> 79.0 mm, vias 0 -> 1
- net /MCU/MB1: track 0.00 -> 78.6 mm, vias 0 -> 4
- net /MCU/MB2: track 0.00 -> 77.1 mm, vias 0 -> 2
- net /Power/VIN: track 75.4 -> 0.00 mm, vias 9 -> 0
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- added copper zone on F.Cu, net /MD/M1PWR
- added copper zone on In2.Cu, net /MD/M1PWR
- added copper zone on In3.Cu, net /MD/M1PWR
- added copper zone on F.Cu, net /MD/M2PWR
- added copper zone on In2.Cu, net /MD/M2PWR
- added copper zone on In3.Cu, net /MD/M2PWR
- added copper zone on B.Cu, net /MD/M3PWR
- added copper zone on F.Cu, net /Power/BATT+
- added copper zone on In2.Cu, net /Power/BATT+
- added copper zone on F.Cu, net /VCC
- added copper zone on In2.Cu, net /VCC
- added copper zone on In1.Cu, net GND
- added copper zone on In2.Cu, net GND
- added copper zone on In3.Cu, net GND
- added copper zone on In4.Cu, net GND
- added copper zone on F.Cu, net Net-(J301-Pin_2)
- added copper zone on In2.Cu, net Net-(J301-Pin_2)
- added copper zone on In4.Cu, net Net-(J301-Pin_2)
- added copper zone on F.Cu, net Net-(J302-Pin_2)
- added copper zone on In1.Cu, net Net-(J302-Pin_2)
- added copper zone on F.Cu, net Net-(J401-Pin_1)
- added copper zone on In2.Cu, net Net-(J401-Pin_1)
- added copper zone on F.Cu, net Net-(J401-Pin_2)
- added copper zone on In2.Cu, net Net-(J401-Pin_2)
- added copper zone on F.Cu, net Net-(J402-Pin_1)
- added copper zone on In2.Cu, net Net-(J402-Pin_1)
- added copper zone on F.Cu, net Net-(J402-Pin_2)
- added copper zone on In2.Cu, net Net-(J402-Pin_2)
- added copper zone on F.Cu, net Net-(L203-Pad1)
- added copper zone on In2.Cu, net Net-(L203-Pad1)
- added copper zone on F.Cu, net Net-(L204-Pad1)
- added copper zone on In2.Cu, net Net-(L204-Pad1)
- added copper zone on F.Cu, net Net-(L205-Pad1)
- added copper zone on In2.Cu, net Net-(L205-Pad1)
- added copper zone on F.Cu, net Net-(L206-Pad1)
- added copper zone on In2.Cu, net Net-(L206-Pad1)
- added copper zone on F.Cu, net Net-(Q307-D)
- added copper zone on In1.Cu, net Net-(Q307-D)
- added copper zone on F.Cu, net Net-(U203-SW)
- added copper zone on F.Cu, net Net-(U206-SW)
- added copper zone on B.Cu, net VIN
- added copper zone on F.Cu, net VIN
- added copper zone on In2.Cu, net VIN
- added copper zone on In3.Cu, net VIN
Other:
- board outline added: 96 x 70 mm
- copper layers 2 -> 6
- board text added: "C&DH Board"
- board text added: "Designed by Denshiruko"
- board text added: "FP"
- board text added: "GND VCC"
- board text added: "GND VIN"
- board text added: "I2C SDA SCL GND"
- board text added: "M3"
- board text added: "MasterSwitch"
- board text added: "Mission Board"
- board text added: "Pri."
- board text added: "Sec."
- board text added: "SoftSwitch"
- board text added: "VCC GND"
- board text added: "VIN GND"
- board text added: "Ver2026.1"
- board text removed: "+"
- board text removed: "B1"
- board text removed: "B2"
- board text removed: "CAM UART"
- board text removed: "CAMERA"
- board text removed: "CdS"
- board text removed: "Flight Pin"
- board text removed: "Heater"
- board text removed: "I2C"
- board text removed: "LPower"
- board text removed: "MCU UART"
- board text removed: "MCUPower"
- board text removed: "MPWM"
- board text removed: "MPower"
- board text removed: "Motor Power"
- board text removed: "Power"
- board text removed: "Power EN"
- board text removed: "UART"
- board text removed: "UART1"
- board text removed: "UART2"
- board text removed: "mSD Card"
